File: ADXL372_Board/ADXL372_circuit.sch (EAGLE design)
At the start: 10 parts, among them U1 STM32F030C8T6, U2 ADXL345BCCZ, U3 ADXL372BCCZ-RL7

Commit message: 回路図一部修正
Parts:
- added C8: (no value), rcl:C-EUC0603K
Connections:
- net +3V3: now also C8.1
- net GND: now also C8.2, U1.VSSA
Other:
- moved on the sheet: C1, C2, C3
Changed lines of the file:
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@@
 <part name="SUPPLY8" library="supply2" library_urn="urn:adsk.eagle:library:372" deviceset="GND" device=""/>
 <part name="SUPPLY9" library="supply2" library_urn="urn:adsk.eagle:library:372" deviceset="GND" device=""/>
+<part name="C8" library="rcl" library_urn="urn:adsk.eagle:library:334" deviceset="C-EU" device="C0603K" package3d_urn="urn:adsk.eagle:package:23680/2"/>
 </parts>
 <sheets>
@@
 <attribute name="VALUE" x="203.2" y="203.2" size="1.778" layer="96"/>
 </instance>
-<instance part="SUPPLY1" gate="GND" x="215.9" y="172.72" smashed="yes">
-<attribute name="VALUE" x="213.995" y="169.545" size="1.778" layer="96"/>
-</instance>
-<instance part="C1" gate="G$1" x="215.9" y="185.42" smashed="yes">
-<attribute name="NAME" x="217.424" y="185.801" size="1.778" layer="95"/>
-<attribute name="VALUE" x="217.424" y="180.721" size="1.778" layer="96"/>
+<instance part="SUPPLY1" gate="GND" x="213.36" y="172.72" smashed="yes">
+<attribute name="VALUE" x="211.455" y="169.545" size="1.778" layer="96"/>
+</instance>
+<instance part="C1" gate="G$1" x="213.36" y="185.42" smashed="yes">
+<attribute name="NAME" x="214.884" y="185.801" size="1.778" layer="95"/>
+<attribute name="VALUE" x="214.884" y="180.721" size="1.778" layer="96"/>
 </instance>
 <instance part="SUPPLY2" gate="GND" x="205.74" y="86.36" smashed="yes">
 <attribute name="VALUE" x="203.835" y="83.185" size="1.778" layer="96"/>
 </instance>
-<instance part="C2" gate="G$1" x="238.76" y="185.42" smashed="yes">
-<attribute name="NAME" x="240.284" y="185.801" size="1.778" layer="95"/>
-<attribute name="VALUE" x="240.284" y="180.721" size="1.778" layer="96"/>
-</instance>
-<instance part="+3V2" gate="G$1" x="231.14" y="200.66" smashed="yes">
-<attribute name="VALUE" x="228.6" y="203.2" size="1.778" layer="96"/>
-</instance>
-<instance part="SUPPLY3" gate="GND" x="238.76" y="172.72" smashed="yes">
-<attribute name="VALUE" x="236.855" y="169.545" size="1.778" layer="96"/>
-</instance>
-<instance part="C3" gate="G$1" x="223.52" y="185.42" smashed="yes">
-<attribute name="NAME" x="225.044" y="185.801" size="1.778" layer="95"/>
-<attribute name="VALUE" x="225.044" y="180.721" size="1.778" layer="96"/>
+<instance part="C2" gate="G$1" x="233.68" y="185.42" smashed="yes">
+<attribute name="NAME" x="235.204" y="185.801" size="1.778" layer="95"/>
+<attribute name="VALUE" x="235.204" y="180.721" size="1.778" layer="96"/>
+</instance>
+<instance part="+3V2" gate="G$1" x="226.06" y="200.66" smashed="yes">
+<attribute name="VALUE" x="223.52" y="203.2" size="1.778" layer="96"/>
+</instance>
+<instance part="SUPPLY3" gate="GND" x="233.68" y="172.72" smashed="yes">
+<attribute name="VALUE" x="231.775" y="169.545" size="1.778" layer="96"/>
+</instance>
+<instance part="C3" gate="G$1" x="241.3" y="185.42" smashed="yes">
+<attribute name="NAME" x="242.824" y="185.801" size="1.778" layer="95"/>
+<attribute name="VALUE" x="242.824" y="180.721" size="1.778" layer="96"/>
 </instance>
 <instance part="U1" gate="G$1" x="172.72" y="129.54" smashed="yes">
@@
 <instance part="SUPPLY9" gate="GND" x="332.74" y="60.96" smashed="yes">
 <attribute name="VALUE" x="330.835" y="57.785" size="1.778" layer="96"/>
+</instance>
+<instance part="C8" gate="G$1" x="248.92" y="185.42" smashed="yes">
+<attribute name="NAME" x="250.444" y="185.801" size="1.778" layer="95"/>
+<attribute name="VALUE" x="250.444" y="180.721" size="1.778" layer="96"/>
 </instance>
 </instances>
@@
 <pinref part="C1" gate="G$1" pin="1"/>
 <wire x1="205.74" y1="193.04" x2="205.74" y2="198.12" width="0.1524" layer="91"/>
-<wire x1="215.9" y1="187.96" x2="215.9" y2="193.04" width="0.1524" layer="91"/>
-<wire x1="215.9" y1="193.04" x2="205.74" y2="193.04" width="0.1524" layer="91"/>
+<wire x1="213.36" y1="187.96" x2="213.36" y2="193.04" width="0.1524" layer="91"/>
+<wire x1="213.36" y1="193.04" x2="205.74" y2="193.04" width="0.1524" layer="91"/>
 <junction x="205.74" y="193.04"/>
-<wire x1="215.9" y1="193.04" x2="223.52" y2="193.04" width="0.1524" layer="91"/>
-<junction x="215.9" y="193.04"/>
+<pinref part="U1" gate="G$1" pin="VDDA"/>
+</segment>
+<segment>
+<pinref part="+3V2" gate="G$1" pin="+3V3"/>
+<wire x1="198.12" y1="165.1" x2="226.06" y2="165.1" width="0.1524" layer="91"/>
+<wire x1="226.06" y1="165.1" x2="226.06" y2="190.5" width="0.1524" layer="91"/>
+<pinref part="C2" gate="G$1" pin="1"/>
+<wire x1="226.06" y1="190.5" x2="226.06" y2="198.12" width="0.1524" layer="91"/>
+<wire x1="233.68" y1="187.96" x2="233.68" y2="190.5" width="0.1524" layer="91"/>
+<wire x1="233.68" y1="190.5" x2="226.06" y2="190.5" width="0.1524" layer="91"/>
+<junction x="226.06" y="190.5"/>
+<pinref part="U1" gate="G$1" pin="VDD"/>
+<pinref part="C8" gate="G$1" pin="1"/>
+<wire x1="248.92" y1="187.96" x2="248.92" y2="190.5" width="0.1524" layer="91"/>
+<wire x1="248.92" y1="190.5" x2="241.3" y2="190.5" width="0.1524" layer="91"/>
+<junction x="233.68" y="190.5"/>
 <pinref part="C3" gate="G$1" pin="1"/>
-<wire x1="223.52" y1="187.96" x2="223.52" y2="193.04" width="0.1524" layer="91"/>
-<pinref part="U1" gate="G$1" pin="VDDA"/>
-</segment>
-<segment>
-<pinref part="+3V2" gate="G$1" pin="+3V3"/>
-<wire x1="198.12" y1="165.1" x2="231.14" y2="165.1" width="0.1524" layer="91"/>
-<wire x1="231.14" y1="165.1" x2="231.14" y2="190.5" width="0.1524" layer="91"/>
-<pinref part="C2" gate="G$1" pin="1"/>
-<wire x1="231.14" y1="190.5" x2="231.14" y2="198.12" width="0.1524" layer="91"/>
-<wire x1="238.76" y1="187.96" x2="238.76" y2="190.5" width="0.1524" layer="91"/>
-<wire x1="238.76" y1="190.5" x2="231.14" y2="190.5" width="0.1524" layer="91"/>
-<junction x="231.14" y="190.5"/>
-<pinref part="U1" gate="G$1" pin="VDD"/>
+<wire x1="241.3" y1="190.5" x2="233.68" y2="190.5" width="0.1524" layer="91"/>
+<wire x1="241.3" y1="187.96" x2="241.3" y2="190.5" width="0.1524" layer="91"/>
+<junction x="241.3" y="190.5"/>
 </segment>
 <segment>
@@
 <pinref part="C1" gate="G$1" pin="2"/>
 <pinref part="SUPPLY1" gate="GND" pin="GND"/>
-<wire x1="215.9" y1="180.34" x2="215.9" y2="177.8" width="0.1524" layer="91"/>
-<wire x1="215.9" y1="177.8" x2="215.9" y2="175.26" width="0.1524" layer="91"/>
-<wire x1="215.9" y1="177.8" x2="223.52" y2="177.8" width="0.1524" layer="91"/>
-<junction x="215.9" y="177.8"/>
-<pinref part="C3" gate="G$1" pin="2"/>
-<wire x1="223.52" y1="180.34" x2="223.52" y2="177.8" width="0.1524" layer="91"/>
+<wire x1="213.36" y1="180.34" x2="213.36" y2="175.26" width="0.1524" layer="91"/>
 </segment>
 <segment>
@@
 <wire x1="205.74" y1="93.98" x2="205.74" y2="88.9" width="0.1524" layer="91"/>
 <pinref part="U1" gate="G$1" pin="VSS"/>
+<pinref part="U1" gate="G$1" pin="VSSA"/>
+<wire x1="198.12" y1="96.52" x2="205.74" y2="96.52" width="0.1524" layer="91"/>
+<wire x1="205.74" y1="96.52" x2="205.74" y2="93.98" width="0.1524" layer="91"/>
+<junction x="205.74" y="93.98"/>
 </segment>
 <segment>
 <pinref part="SUPPLY3" gate="GND" pin="GND"/>
 <pinref part="C2" gate="G$1" pin="2"/>
-<wire x1="238.76" y1="175.26" x2="238.76" y2="180.34" width="0.1524" layer="91"/>
-</segment>
-<segment>
+<wire x1="233.68" y1="175.26" x2="233.68" y2="177.8" width="0.1524" layer="91"/>
+<pinref part="C3" gate="G$1" pin="2"/>
+<wire x1="233.68" y1="177.8" x2="233.68" y2="180.34" width="0.1524" layer="91"/>
+<wire x1="241.3" y1="180.34" x2="241.3" y2="177.8" width="0.1524" layer="91"/>
+<wire x1="241.3" y1="177.8" x2="233.68" y2="177.8" width="0.1524" layer="91"/>
+<junction x="233.68" y="177.8"/>
+<pinref part="C8" gate="G$1" pin="2"/>
+<wire x1="248.92" y1="180.34" x2="248.92" y2="177.8" width="0.1524" layer="91"/>
+<wire x1="248.92" y1="177.8" x2="241.3" y2="177.8" width="0.1524" layer="91"/>
+<junction x="241.3" y="177.8"/>
+</segment>
+<segment>

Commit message: Add Parts
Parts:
- added BT1: BU2032SM-HD-G, BU2032SM-HD-G:BU2032SM-HD-G
- added C10, C9: 8pf, OPL_Capacitor:CERAMIC-10PF-50V-5%-NPO(0603)
- added C11, C13, C14, C16, C17, C18: 100nf, OPL_Capacitor:CERAMIC-100NF-50V-10%-X7R(0603)
- added C12: 1uf, OPL_Capacitor:CERAMIC-1UF-25V-10%-X7R(0805)
- added C15, C19: 10uf, OPL_Capacitor:CERAMIC-10UF-10V-(-20%～+80%)-Y5V(0805)
- added C20, C21: 12.5pf, OPL_Capacitor:CERAMIC-10PF-50V-5%-NPO(0603)
- added D1: BLUE-0603, Seeed-LED:SMD-LED-CLEAR-BLUE(0603)
- added IC4: SI7006-A20-IM, SI7006-A20-IM:SI7006-A20-IM
- added IC5: LP5907MFX-2.5/NOPB, LP5907MFX-2.5_NOPB:LP5907MFX-2.5/NOPB
- added R1: 470R, OPL_Resistor:SMD-RES-470R-5%-1/10W(0603)
- added R2, R3: 10K 1/10W, OPL_Resistor:SMD-RES-10K-5%-1/10W(0603)
- added SW1: DHT-4235A, OPL_Switch:SMD-BUTTON-TOP-DHT-4235A(4P-4.2X3.2MM)
- added U$1: STM32L051C6, stm32l05x6:STM32L051C6
- added Y1: 16MHZ_X053201602002, OPL_Crystal Oscillator:SMD-CRYSTAL-16MHZ-8PF-20PPM-40R(2P-5.0X3.2MM)
- added Y2: 3.2768KHZ, OPL_Crystal Oscillator:SMD-CRYSTAL-32.768KHZ-12.5PF-20PPM-90K(2P-L2.0X1.2MM)
- C1, C3: value (none) -> 10uf; device rcl:C-EUC0603K -> OPL_Capacitor:CERAMIC-10UF-10V-(-20%～+80%)-Y5V(0805)
- C2, C8: value (none) -> 100nf; device rcl:C-EUC0603K -> OPL_Capacitor:CERAMIC-100NF-50V-10%-X7R(0603)
- C4, C6: value 0.1μ -> 100nf; device rcl:C-EUC0603K -> OPL_Capacitor:CERAMIC-100NF-50V-10%-X7R(0603)
- C5: value 1μ -> 100nf; device rcl:C-EUC0603K -> OPL_Capacitor:CERAMIC-100NF-50V-10%-X7R(0603)
- C7: value 0.1μ -> 10uf; device rcl:C-EUC0603K -> OPL_Capacitor:CERAMIC-10UF-10V-(-20%～+80%)-Y5V(0805)
- U1: value STM32F030C8T6 -> MX25R1635FM1IL0; device STM32F030C8T6:STM32F030C8T6 -> MX25R1635FM1IL0:MX25R1635FM1IL0
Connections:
- new net +2V5: C1.2, C11.2, C12.2, C15.2, C18.2, C19.2, C2.2, C3.2, C7.2, C8.2, IC5.OUT, U$1.VDD, U$1.VDDA
- new net ADXL345_CS: U$1.PA8
- new net ADXL372_CS: U$1.PA9
- new net I2C1_SCL: U$1.PB8
- new net I2C1_SDA: U$1.PB9
- new net I2C2_SCL: IC4.SCL, R2.1, U$1.PB13
- new net I2C2_SDA: IC4.SDA, R3.1, U$1.PB14
- new net N$1: C9.2, U$1.PC14-OSC32_IN, Y1.2
- new net N$10: U2.SDA/SDI/SDIO
- new net N$11: U2.SDO/ALT_ADDRESS
- new net N$12: U3.INT1
- new net N$13: U3.INT2
- new net N$14: C20.1, U$1.PH0-OSC_IN, Y2.2
- new net N$15: C21.1, U$1.PH1-OSC_OUT, Y2.1
- new net N$16: U$1.PA10
- new net N$19: R1.2, U$1.PA0
- new net N$2: C10.2, U$1.PC15-OSC32_OUT, Y1.1
- new net N$20: D1.+, R1.1
- new net N$22: BT1.+, IC5.IN
- new net N$24: U1.CS#
- new net N$3: C13.2, SW1.A0, U$1.NRST
- new net N$4: U2.SCL/SCLK
- new net N$5: U3.SCLK
- new net N$6: U3.!CS!/SCL
- new net N$7: U3.MOSI/SDA
- new net N$8: U3.MISO
- new net N$9: U2.*CS
- new net SPI1_MISO: U$1.PA6, U1.SO/SIO1
- new net SPI1_MOSI: U$1.PA7, U1.SI/SIO0
- new net SPI1_SCK: U$1.PA5, U1.SCLK
- net +3V3: now also C14.2, C16.2, C17.2, C4.2, C5.2, C6.2, IC4.VDD, R2.2, R3.2, U1.VCC; no longer C1.1, C2.1, C3.1, C4.1, C5.1, C6.1, C7.1, C8.1, U1.VDD, U1.VDDA
- net GND: now also BT1.-, C1.1, C10.1, C11.1, C12.1, C13.1, C14.1, C15.1, C16.1, C17.1, C18.1, C19.1, C2.1, C20.2, C21.2, C3.1, C4.1, C5.1, C6.1, C7.1, C8.1, C9.1, D1.-, IC4.GND, IC4.TGND, IC5.GND, SW1.B0, SW1.B1, U$1.VSS, U1.GND; no longer C1.2, C2.2, C3.2, C4.2, C5.2, C6.2, C7.2, C8.2, U1.VSS, U1.VSSA
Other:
- note added: "Low drop out"
- moved on the sheet: U2, U3

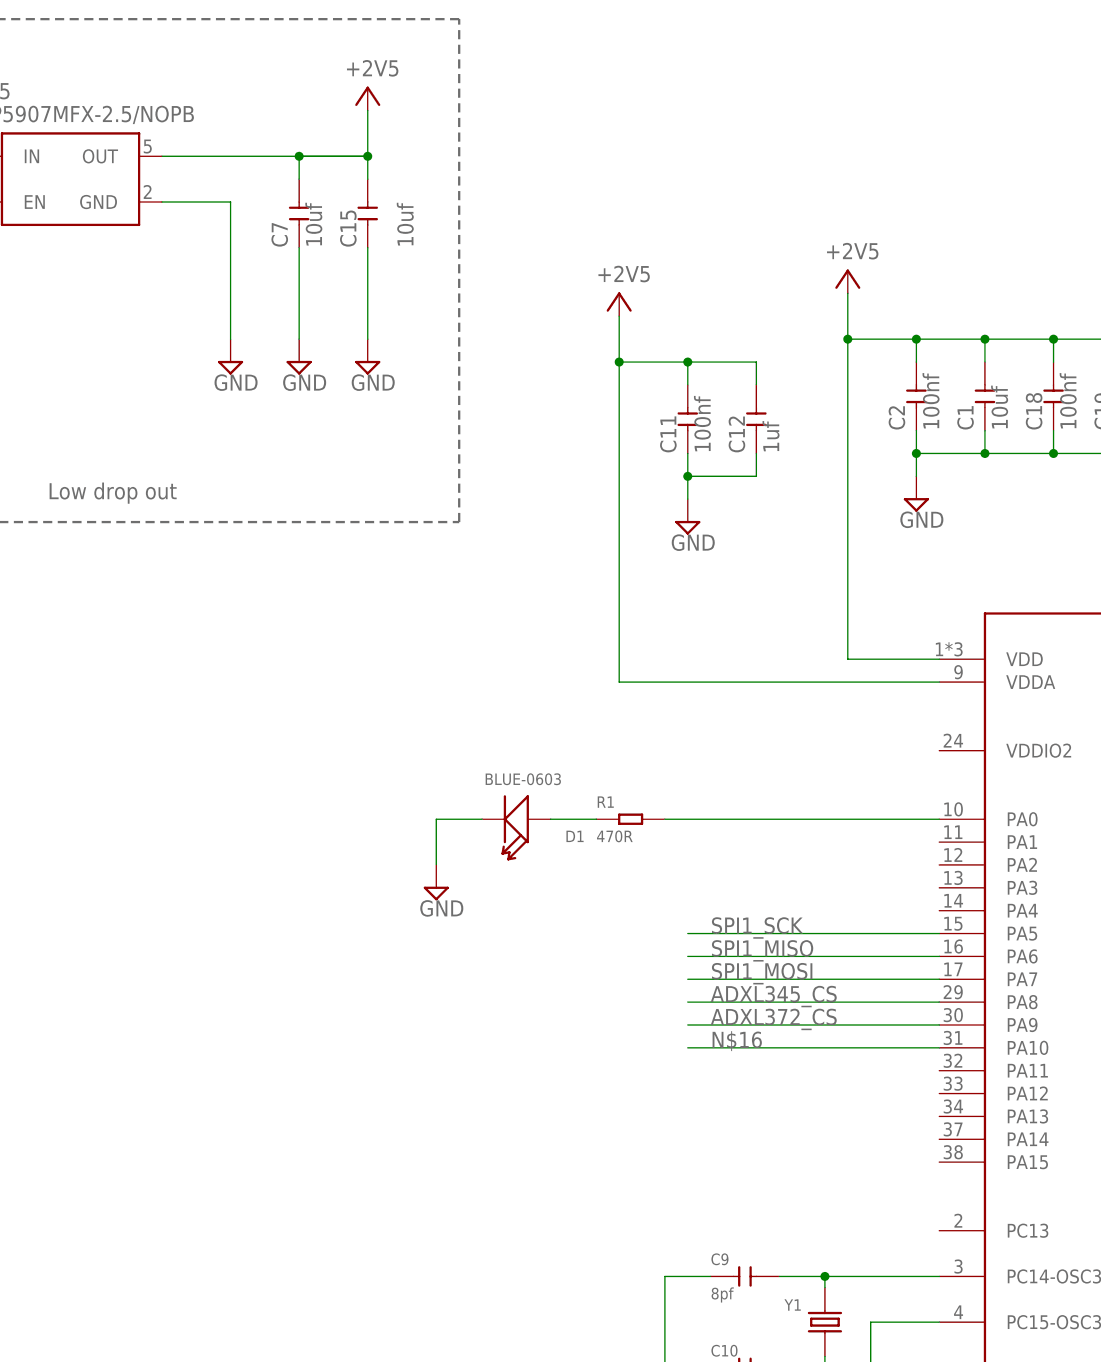
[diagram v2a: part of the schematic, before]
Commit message: LED駆動用FETを追加
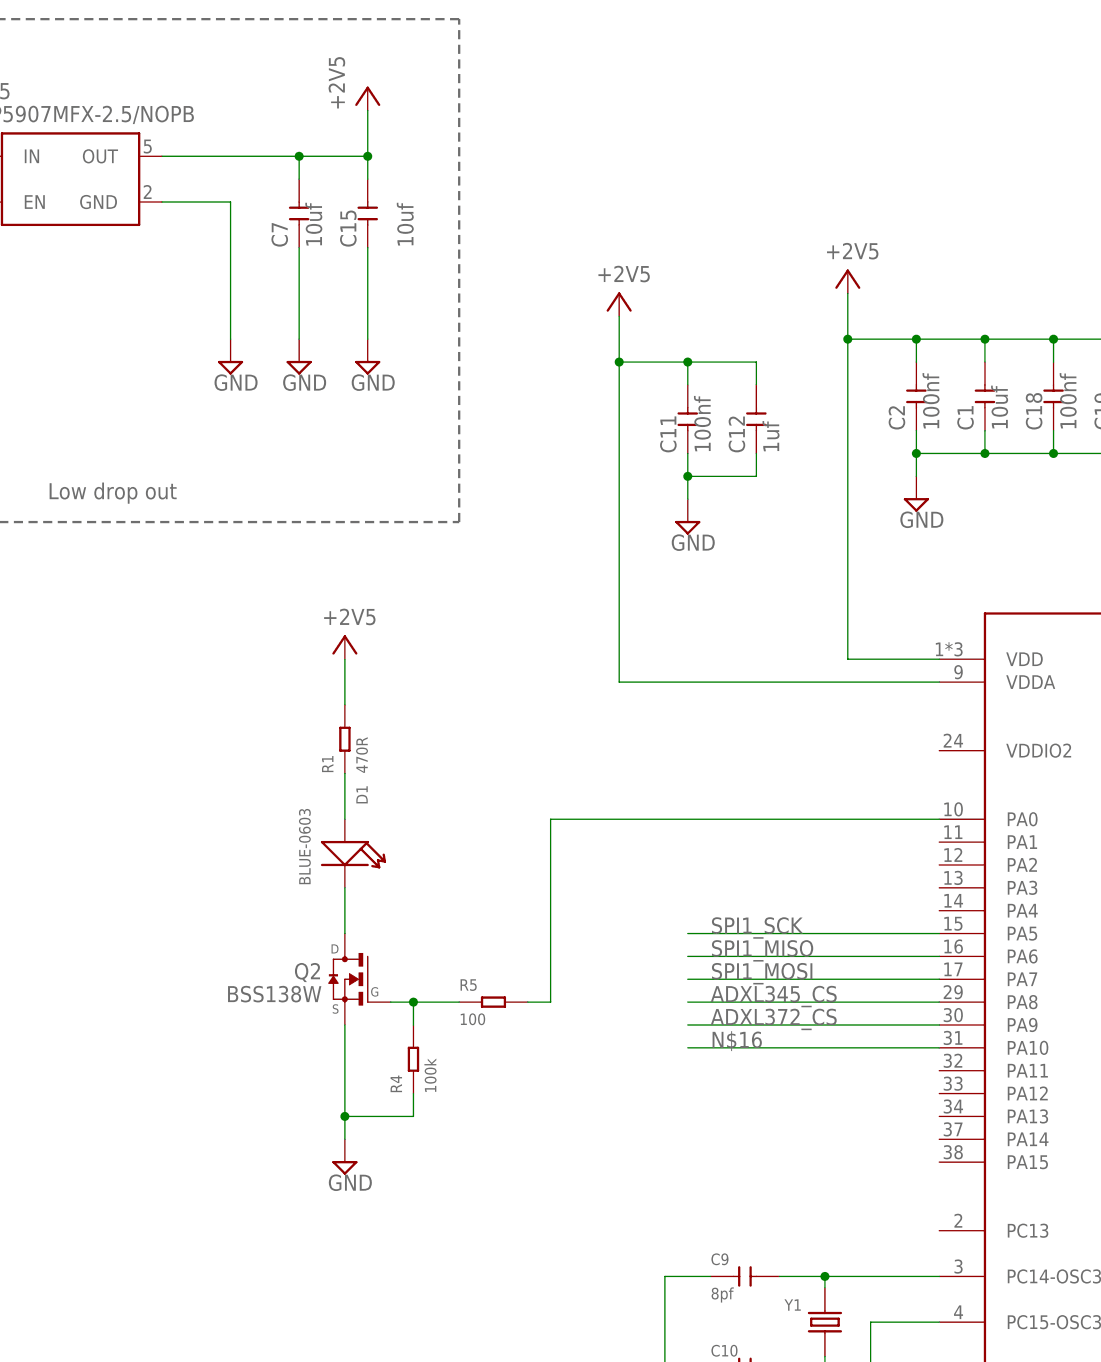
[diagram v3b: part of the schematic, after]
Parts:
- added Q2: BSS138W, BSS138W:BSS138W
- added R4: 100k, OPL_Resistor:SMD-RES-470R-5%-1/10W(0603)
- added R5: 100, OPL_Resistor:SMD-RES-470R-5%-1/10W(0603)
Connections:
- new net N$17: R5.2, U$1.PA0
- new net N$20: Q2.G, R4.2, R5.1
- new net VCC: C15.2, C7.2, IC5.OUT
- net +2V5: no longer C15.2, C7.2, IC5.OUT
- net +3V3: now also R1.2
- net GND: now also Q2.S, R4.1; no longer D1.-
- net N$19: now also D1.-, Q2.D; no longer R1.2, U$1.PA0
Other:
- moved on the sheet: D1, R1
